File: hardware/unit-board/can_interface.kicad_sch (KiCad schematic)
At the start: 8 parts, among them J4 SM03B-GHS-TB, J5 SM03B-GHS-TB, SW2 JS102011SAQN, U5 TCAN1051VDRQ1

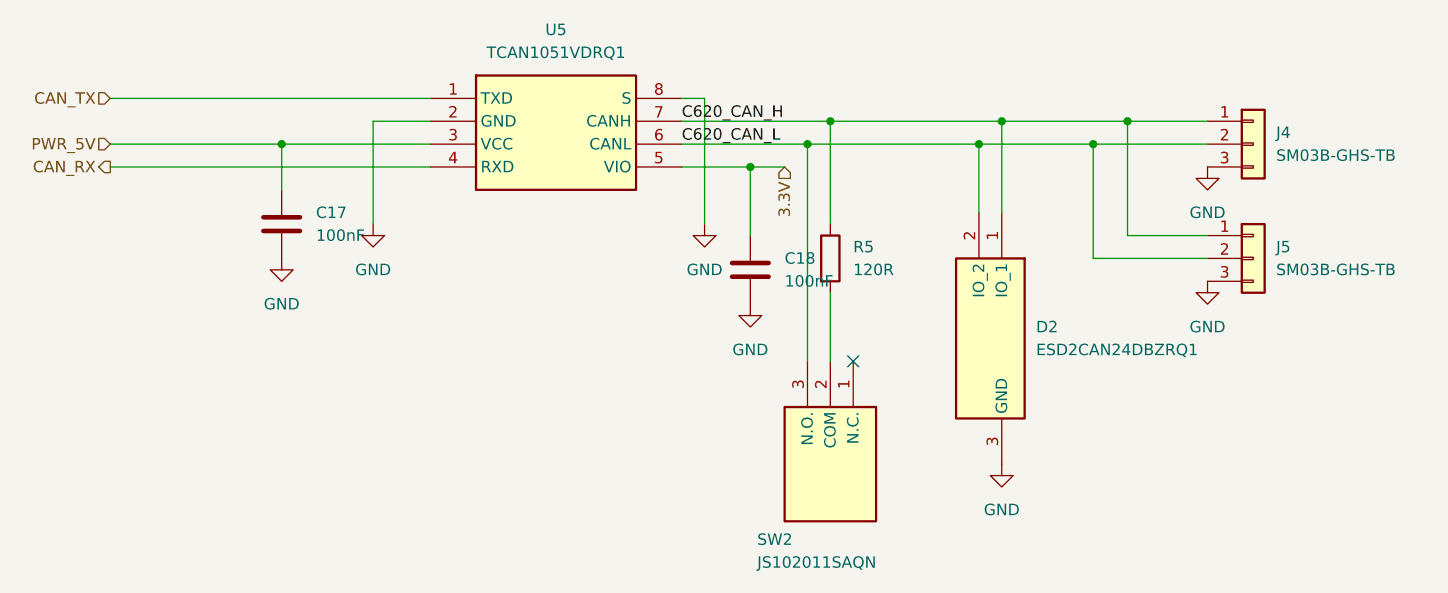
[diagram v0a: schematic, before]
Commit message: chore(hardware): update unit board design
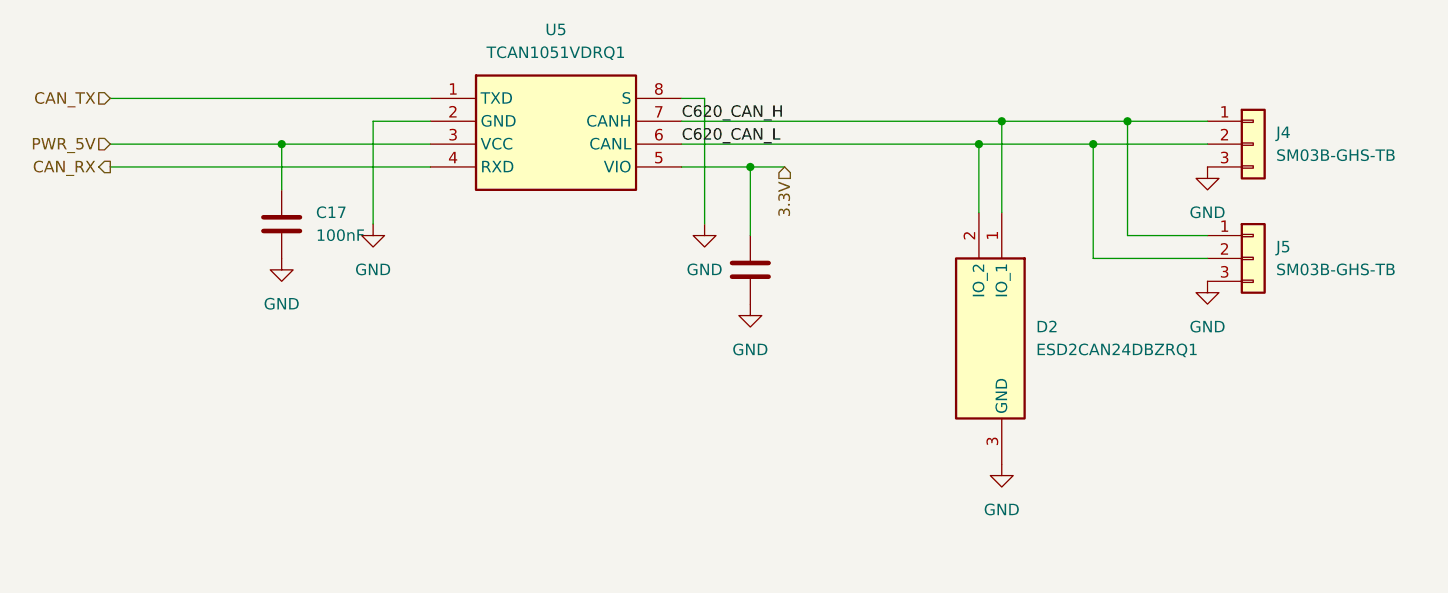
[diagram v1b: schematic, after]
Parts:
- removed R5: 120R, Resistor_SMD:R_0603_1608Metric, symbol Device:R
- removed SW2: JS102011SAQN, DifferentialSwerve:JS102011SAQN, symbol DifferentialSwerve:JS102011SAQN
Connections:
- no-connect marks 1 -> 0
